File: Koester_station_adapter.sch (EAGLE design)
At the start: 9 parts, among them CON1 Speaker

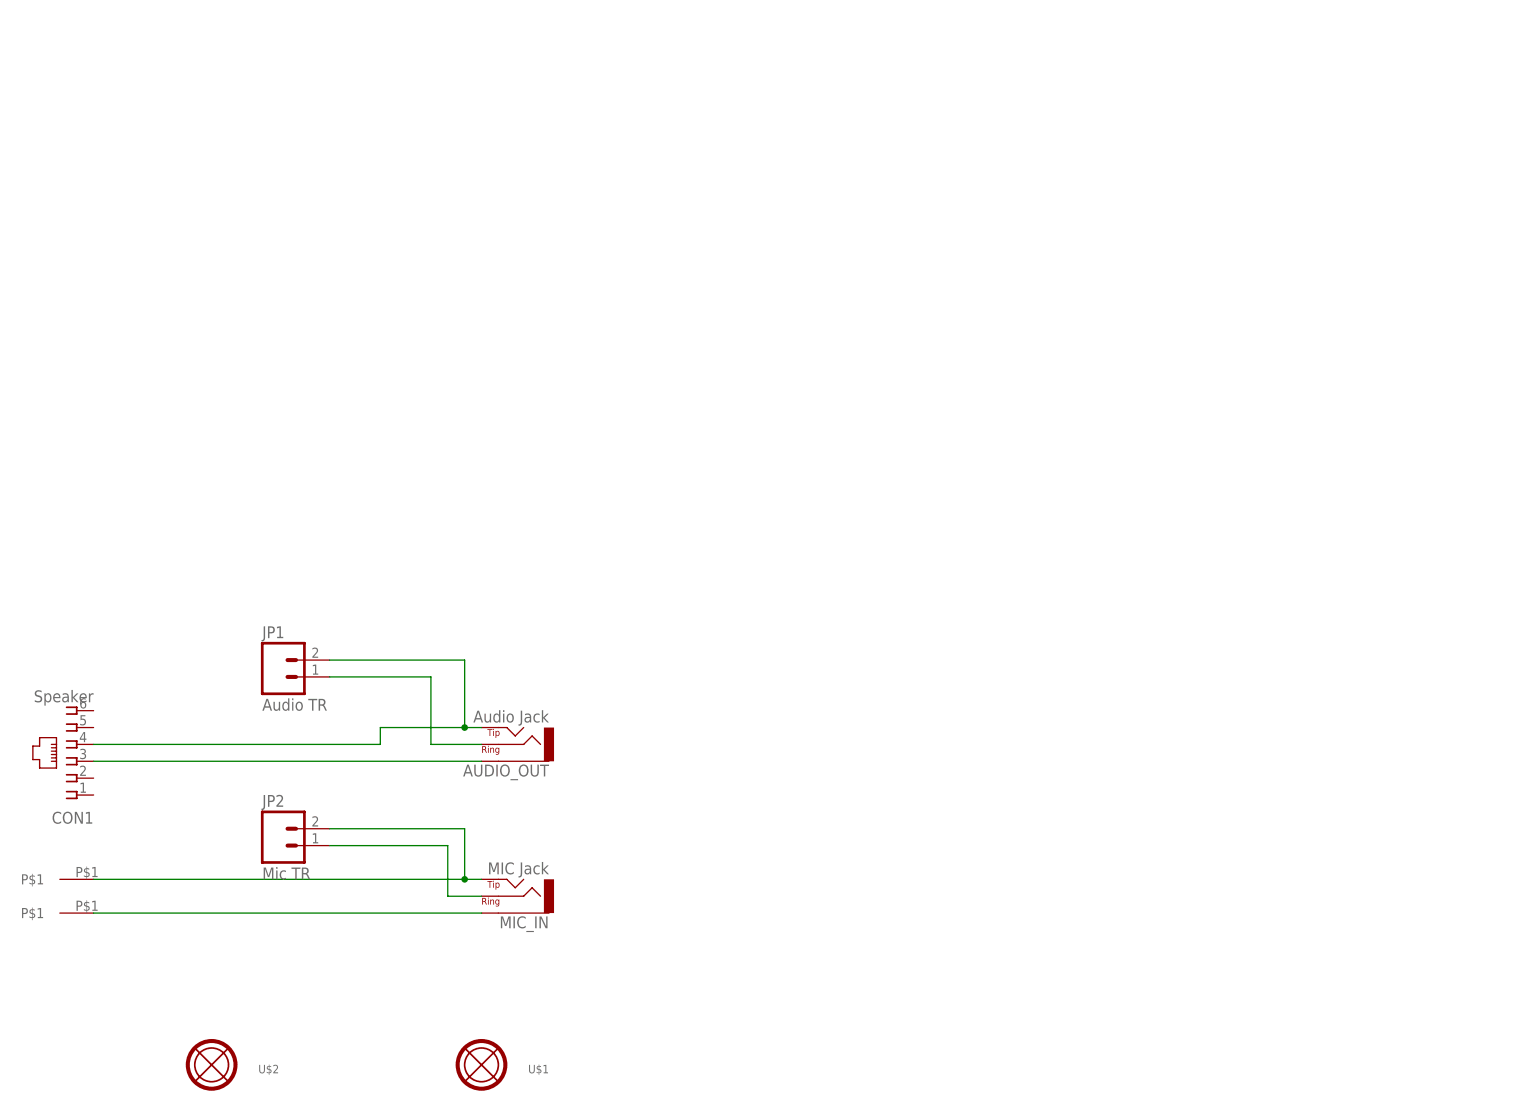
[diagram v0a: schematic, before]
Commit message: Version 1.2
Replaced brass screws on board with 6mm terminal strip
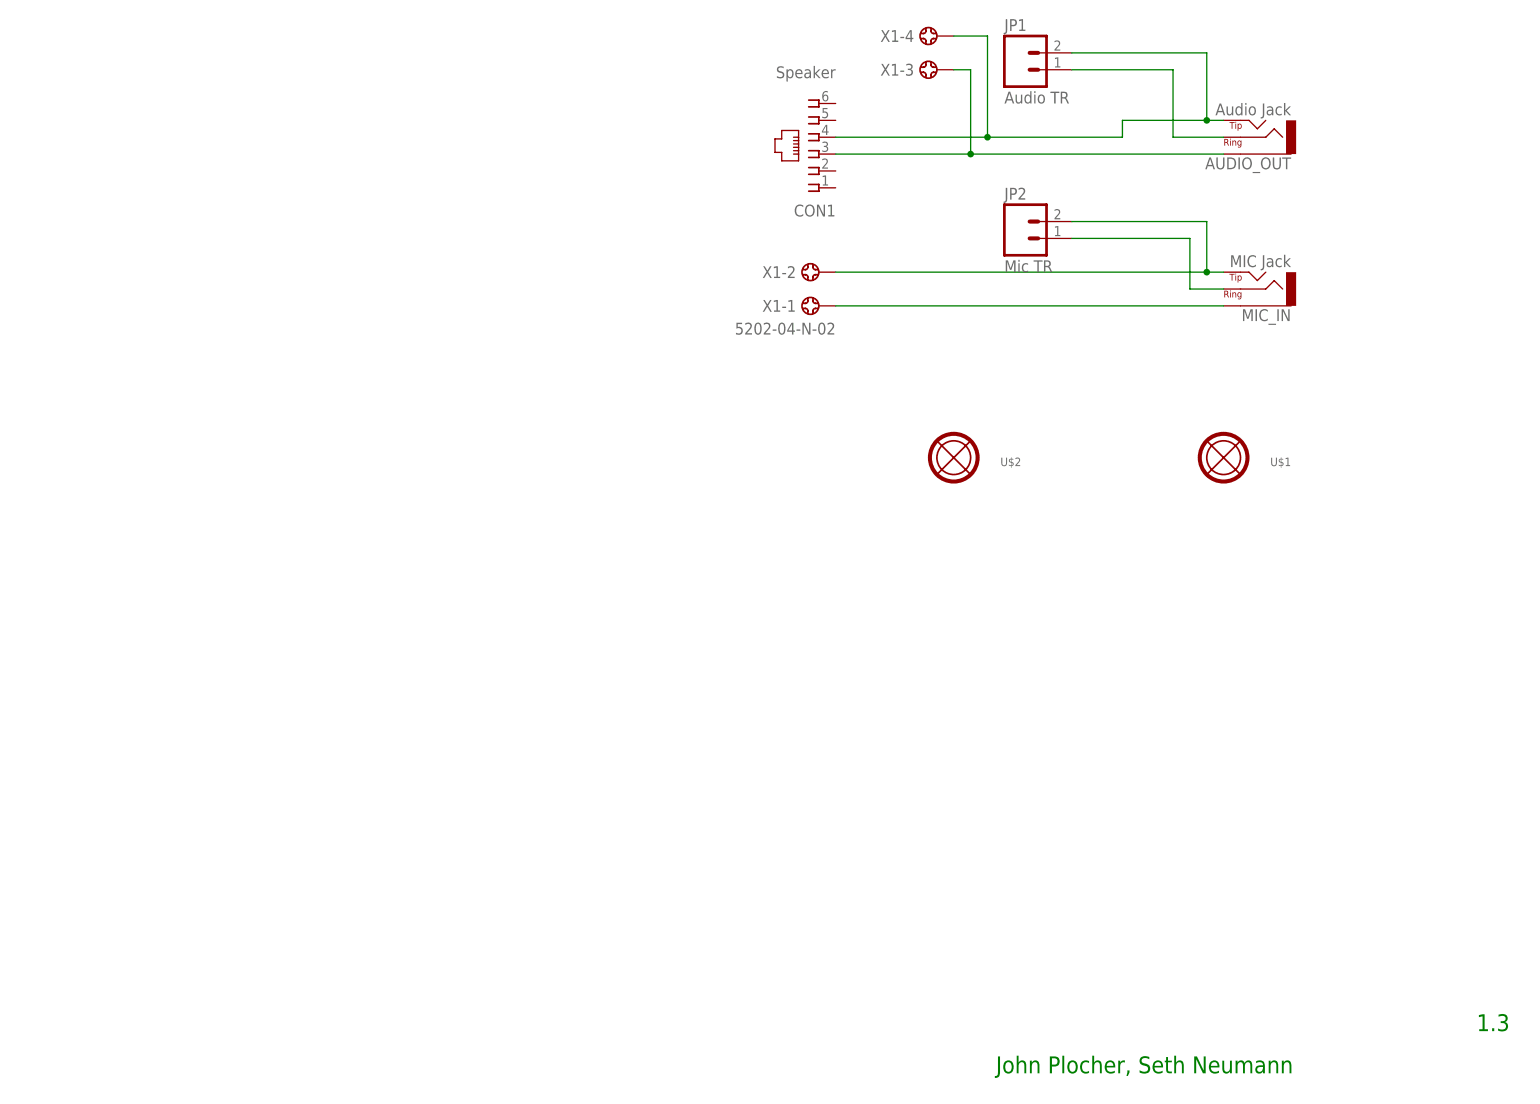
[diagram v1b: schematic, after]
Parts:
- removed U$3: Mic Tip, SPCoast:TP
- removed U$4: TP, SPCoast:TP
- added X1: 5202-04-N-02, con-ebyelectro:5202-04-N-02
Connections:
- removed net N$1: AUDIO_OUT.TIP, CON1.4, JP1.B
- removed net N$2: AUDIO_OUT.SLEEVE, CON1.3
- removed net N$4: MIC_IN.SLEEVE, U$4.P$1
- removed net N$5: JP2.B, MIC_IN.TIP, U$3.P$1
- new net MIC_SLEEVE: MIC_IN.SLEEVE, X1-1.1
- new net MIC_TIP: JP2.B, MIC_IN.TIP, X1-2.1
- new net OUT_SLEEVE: AUDIO_OUT.SLEEVE, CON1.3, X1-3.1
- new net OUT_TIP: AUDIO_OUT.TIP, CON1.4, JP1.B, X1-4.1
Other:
- note added: "1.3"
- note added: "John Plocher, Seth Neumann"
- moved on the sheet: AUDIO_OUT, CON1, JP1, JP2, MIC_IN, U$1, U$2
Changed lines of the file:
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@@
 <?xml version="1.0" encoding="utf-8"?>
 <!DOCTYPE eagle SYSTEM "eagle.dtd">
-<eagle version="7.3.0">
+<eagle version="7.7.0">
 <drawing>
 <settings>
@@
 <part name="JP1" library="SPCoast" deviceset="CONNECTOR-M02" device="MOLEX-1X02-LOCK" value="Audio TR"/>
 <part name="JP2" library="SPCoast" deviceset="CONNECTOR-M02" device="MOLEX-1X02-LOCK" value="Mic TR"/>
-<part name="U$3" library="SPCoast" deviceset="TP" device="" value="Mic Tip"/>
-<part name="U$4" library="SPCoast" deviceset="TP" device=""/>
+<part name="X1" library="con-ebyelectro" deviceset="5202-04-N-02" device=""/>
+<part name="FRAME1" library="SPCoast" deviceset="DOC-FRAME-LETTER" device=""/>
 </parts>
 <sheets>
 <sheet>
 <plain>
+<text x="265.43" y="54.61" size="2.54" layer="91">John Plocher, Seth Neumann</text>
+<text x="337.82" y="60.96" size="2.54" layer="91">1.3</text>
 </plain>
 <instances>
-<instance part="CON1" gate="J" x="127" y="101.6" rot="R180"/>
-<instance part="U$1" gate="MT1" x="187.96" y="55.88" rot="R180"/>
-<instance part="U$2" gate="MT1" x="147.32" y="55.88" rot="R180"/>
-<instance part="AUDIO_OUT" gate="J" x="193.04" y="104.14" rot="R180"/>
-<instance part="MIC_IN" gate="J" x="193.04" y="81.28" rot="R180"/>
-<instance part="JP1" gate="J" x="160.02" y="114.3"/>
-<instance part="JP2" gate="J" x="160.02" y="88.9"/>
-<instance part="U$3" gate="G$1" x="129.54" y="83.82" rot="R180"/>
-<instance part="U$4" gate="G$1" x="129.54" y="78.74" rot="R180"/>
+<instance part="CON1" gate="J" x="238.76" y="193.04" smashed="yes" rot="R180">
+<attribute name="NAME" x="241.3" y="185.42" size="1.778" layer="95" rot="R180"/>
+<attribute name="VALUE" x="241.3" y="206.248" size="1.778" layer="96" rot="R180"/>
+</instance>
+<instance part="U$1" gate="MT1" x="299.72" y="147.32" rot="R180"/>
+<instance part="U$2" gate="MT1" x="259.08" y="147.32" rot="R180"/>
+<instance part="AUDIO_OUT" gate="J" x="304.8" y="195.58" rot="R180"/>
+<instance part="MIC_IN" gate="J" x="304.8" y="172.72" rot="R180"/>
+<instance part="JP1" gate="J" x="271.78" y="205.74"/>
+<instance part="JP2" gate="J" x="271.78" y="180.34"/>
+<instance part="X1" gate="-1" x="238.76" y="170.18" rot="R180"/>
+<instance part="X1" gate="-2" x="238.76" y="175.26" rot="R180"/>
+<instance part="X1" gate="-3" x="256.54" y="205.74" rot="R180"/>
+<instance part="X1" gate="-4" x="256.54" y="210.82" rot="R180"/>
+<instance part="FRAME1" gate="FRAME" x="96.52" y="48.26"/>
+<instance part="FRAME1" gate="FRAME_CONTENT" x="243.84" y="48.26"/>
 </instances>
 <busses>
 </busses>
 <nets>
-<net name="N$1" class="0">
+<net name="OUT_TIP" class="0">
 <segment>
 <pinref part="CON1" gate="J" pin="4"/>
-<wire x1="129.54" y1="104.14" x2="172.72" y2="104.14" width="0.3048" layer="91"/>
-<wire x1="172.72" y1="104.14" x2="172.72" y2="106.68" width="0.3048" layer="91"/>
+<wire x1="241.3" y1="195.58" x2="264.16" y2="195.58" width="0.3048" layer="91"/>
+<wire x1="264.16" y1="195.58" x2="284.48" y2="195.58" width="0.3048" layer="91"/>
+<wire x1="284.48" y1="195.58" x2="284.48" y2="198.12" width="0.3048" layer="91"/>
 <pinref part="AUDIO_OUT" gate="J" pin="TIP"/>
-<wire x1="172.72" y1="106.68" x2="185.42" y2="106.68" width="0.3048" layer="91"/>
+<wire x1="284.48" y1="198.12" x2="297.18" y2="198.12" width="0.3048" layer="91"/>
 <pinref part="JP1" gate="J" pin="B"/>
-<wire x1="185.42" y1="106.68" x2="187.96" y2="106.68" width="0.000153125" layer="91"/>
-<wire x1="165.1" y1="116.84" x2="185.42" y2="116.84" width="0.3048" layer="91"/>
-<wire x1="185.42" y1="116.84" x2="185.42" y2="106.68" width="0.3048" layer="91"/>
-<junction x="185.42" y="106.68"/>
-</segment>
-</net>
-<net name="N$2" class="0">
+<wire x1="297.18" y1="198.12" x2="299.72" y2="198.12" width="0.3048" layer="91"/>
+<wire x1="276.86" y1="208.28" x2="297.18" y2="208.28" width="0.3048" layer="91"/>
+<wire x1="297.18" y1="208.28" x2="297.18" y2="198.12" width="0.3048" layer="91"/>
+<junction x="297.18" y="198.12"/>
+<pinref part="X1" gate="-4" pin="1"/>
+<wire x1="259.08" y1="210.82" x2="264.16" y2="210.82" width="0.3048" layer="91"/>
+<wire x1="264.16" y1="210.82" x2="264.16" y2="195.58" width="0.3048" layer="91"/>
+<junction x="264.16" y="195.58"/>
+</segment>
+</net>
+<net name="OUT_SLEEVE" class="0">
 <segment>
 <pinref part="CON1" gate="J" pin="3"/>
 <pinref part="AUDIO_OUT" gate="J" pin="SLEEVE"/>
-<wire x1="129.54" y1="101.6" x2="187.96" y2="101.6" width="0.3048" layer="91"/>
+<wire x1="241.3" y1="193.04" x2="261.62" y2="193.04" width="0.3048" layer="91"/>
+<pinref part="X1" gate="-3" pin="1"/>
+<wire x1="261.62" y1="193.04" x2="299.72" y2="193.04" width="0.3048" layer="91"/>
+<wire x1="259.08" y1="205.74" x2="261.62" y2="205.74" width="0.3048" layer="91"/>
+<wire x1="261.62" y1="205.74" x2="261.62" y2="193.04" width="0.3048" layer="91"/>
+<junction x="261.62" y="193.04"/>
 </segment>
 </net>
@@
 <segment>
 <pinref part="JP1" gate="J" pin="A"/>
-<wire x1="165.1" y1="114.3" x2="180.34" y2="114.3" width="0.3048" layer="91"/>
-<wire x1="180.34" y1="114.3" x2="180.34" y2="104.14" width="0.3048" layer="91"/>
+<wire x1="276.86" y1="205.74" x2="292.1" y2="205.74" width="0.3048" layer="91"/>
+<wire x1="292.1" y1="205.74" x2="292.1" y2="195.58" width="0.3048" layer="91"/>
 <pinref part="AUDIO_OUT" gate="J" pin="RING"/>
-<wire x1="180.34" y1="104.14" x2="187.96" y2="104.14" width="0.3048" layer="91"/>
-</segment>
-</net>
-<net name="N$4" class="0">
-<segment>
-<pinref part="U$4" gate="G$1" pin="P$1"/>
+<wire x1="292.1" y1="195.58" x2="299.72" y2="195.58" width="0.3048" layer="91"/>
+</segment>
+</net>
+<net name="MIC_SLEEVE" class="0">
+<segment>
 <pinref part="MIC_IN" gate="J" pin="SLEEVE"/>
-<wire x1="129.54" y1="78.74" x2="187.96" y2="78.74" width="0.3048" layer="91"/>
-</segment>
-</net>
-<net name="N$5" class="0">
-<segment>
-<pinref part="U$3" gate="G$1" pin="P$1"/>
+<wire x1="241.3" y1="170.18" x2="299.72" y2="170.18" width="0.3048" layer="91"/>
+<pinref part="X1" gate="-1" pin="1"/>
+</segment>
+</net>
+<net name="MIC_TIP" class="0">
+<segment>
 <pinref part="MIC_IN" gate="J" pin="TIP"/>
-<wire x1="129.54" y1="83.82" x2="185.42" y2="83.82" width="0.3048" layer="91"/>
+<wire x1="241.3" y1="175.26" x2="297.18" y2="175.26" width="0.3048" layer="91"/>
 <pinref part="JP2" gate="J" pin="B"/>
-<wire x1="185.42" y1="83.82" x2="187.96" y2="83.82" width="0.000153125" layer="91"/>
-<wire x1="165.1" y1="91.44" x2="185.42" y2="91.44" width="0.3048" layer="91"/>
-<wire x1="185.42" y1="91.44" x2="185.42" y2="83.82" width="0.3048" layer="91"/>
-<junction x="185.42" y="83.82"/>
+<wire x1="297.18" y1="175.26" x2="299.72" y2="175.26" width="0.3048" layer="91"/>
+<wire x1="276.86" y1="182.88" x2="297.18" y2="182.88" width="0.3048" layer="91"/>
+<wire x1="297.18" y1="182.88" x2="297.18" y2="175.26" width="0.3048" layer="91"/>
+<junction x="297.18" y="175.26"/>
+<pinref part="X1" gate="-2" pin="1"/>
 </segment>
 </net>
@@
 <segment>
 <pinref part="JP2" gate="J" pin="A"/>
-<wire x1="165.1" y1="88.9" x2="182.88" y2="88.9" width="0.3048" layer="91"/>
-<wire x1="182.88" y1="88.9" x2="182.88" y2="81.28" width="0.3048" layer="91"/>
+<wire x1="276.86" y1="180.34" x2="294.64" y2="180.34" width="0.3048" layer="91"/>
+<wire x1="294.64" y1="180.34" x2="294.64" y2="172.72" width="0.3048" layer="91"/>
 <pinref part="MIC_IN" gate="J" pin="RING"/>
-<wire x1="182.88" y1="81.28" x2="187.96" y2="81.28" width="0.3048" layer="91"/>
-</segment>
-</net>
+<wire x1="294.64" y1="172.72" x2="299.72" y2="172.72" width="0.3048" layer="91"/>
+</segment>
+</net>
